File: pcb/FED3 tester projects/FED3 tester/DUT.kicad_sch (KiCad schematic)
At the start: 68 parts, among them J3 6pin_hd, J4 Conn_02x03_Odd_Even, J5 MotorCkeck1, J6 MotorCkeck2, J7 Conn_01x02_Socket, K1 Relay SPDT, K2 Relay SPDT, K3 Relay SPDT, Q2 ???????, Q3 DMN63D8L-7, Q4 DMN63D8L-7, Q5 DMN63D8L-7, Q6 DMN63D8L-7, U6 THS4281, U7 THS4281, U8 THS4281, U9 ZXCT1082

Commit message: FED3 tester - sync of the week
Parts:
- added R39: 640k, Resistor_SMD:R_0402_1005Metric, symbol Device:R_US
- added R42: 1M, Resistor_SMD:R_0402_1005Metric, symbol Device:R_US
- R29: value 1.2K -> 1.2K ??
- renumbered C31 to C30, C32 to C31, C33 to C32, C34 to C33, C35 to C34, C36 to C35, C37 to C36, C38 to C37, C39 to C38, R39 to R40, R40 to R41, R41 to R43, R42 to R44, R43 to R45, R44 to R46, R45 to R47, R46 to R48
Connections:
- net GND: now also R42.1
- net LED_CHG: now also R39.1, R42.2; no longer TP10.1
- new net: R39.2, TP10.1
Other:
- moved on the sheet: TP6

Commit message: FED3 tester rev.B & FED3 tester support rev.B
-rev.B para 1ª revisão do Filipe
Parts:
- Q2: value ??????? -> PMF170XP,115; footprint Package_TO_SOT_SMD:SOT-23 -> Package_TO_SOT_SMD:SOT-323_SC-70; MPN (none) -> PMF170XP,115; OEPSPN (none) -> OEPS060012
- renumbered C30 to C29, C31 to C30, C32 to C31, C33 to C32, C34 to C33, C35 to C34, C36 to C35, C37 to C36, C38 to C37, D11 to D10, D12 to D11, D10 to D9, R19 to R18, R20 to R19, R21 to R20, R22 to R21, R23 to R22, R24 to R23, R25 to R24, R26 to R25, R27 to R26, R28 to R27, R29 to R28, R30 to R29, R31 to R30, R32 to R31, R33 to R32, R34 to R33, R35 to R34, R36 to R35, R37 to R36, R38 to R37, R39 to R38, R40 to R39, R41 to R40, R42 to R41, R43 to R42, R44 to R43, R45 to R44, R46 to R45, R47 to R46, R48 to R47
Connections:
- net +3V3test renamed +3V3_DUT
- net DUT_SWCLK renamed SWCLK_DUT
- net DUT_SWDIO renamed SWDIO_DUT
- net ExtVUSB renamed ExtVUSB_DUT
- net ThermalPin renamed ThermalPin_DUT
- net VBattest renamed VBatt_DUT
- net VUSB_out renamed VUSB_DUT
- net VccRGB renamed VccRGB_DUT

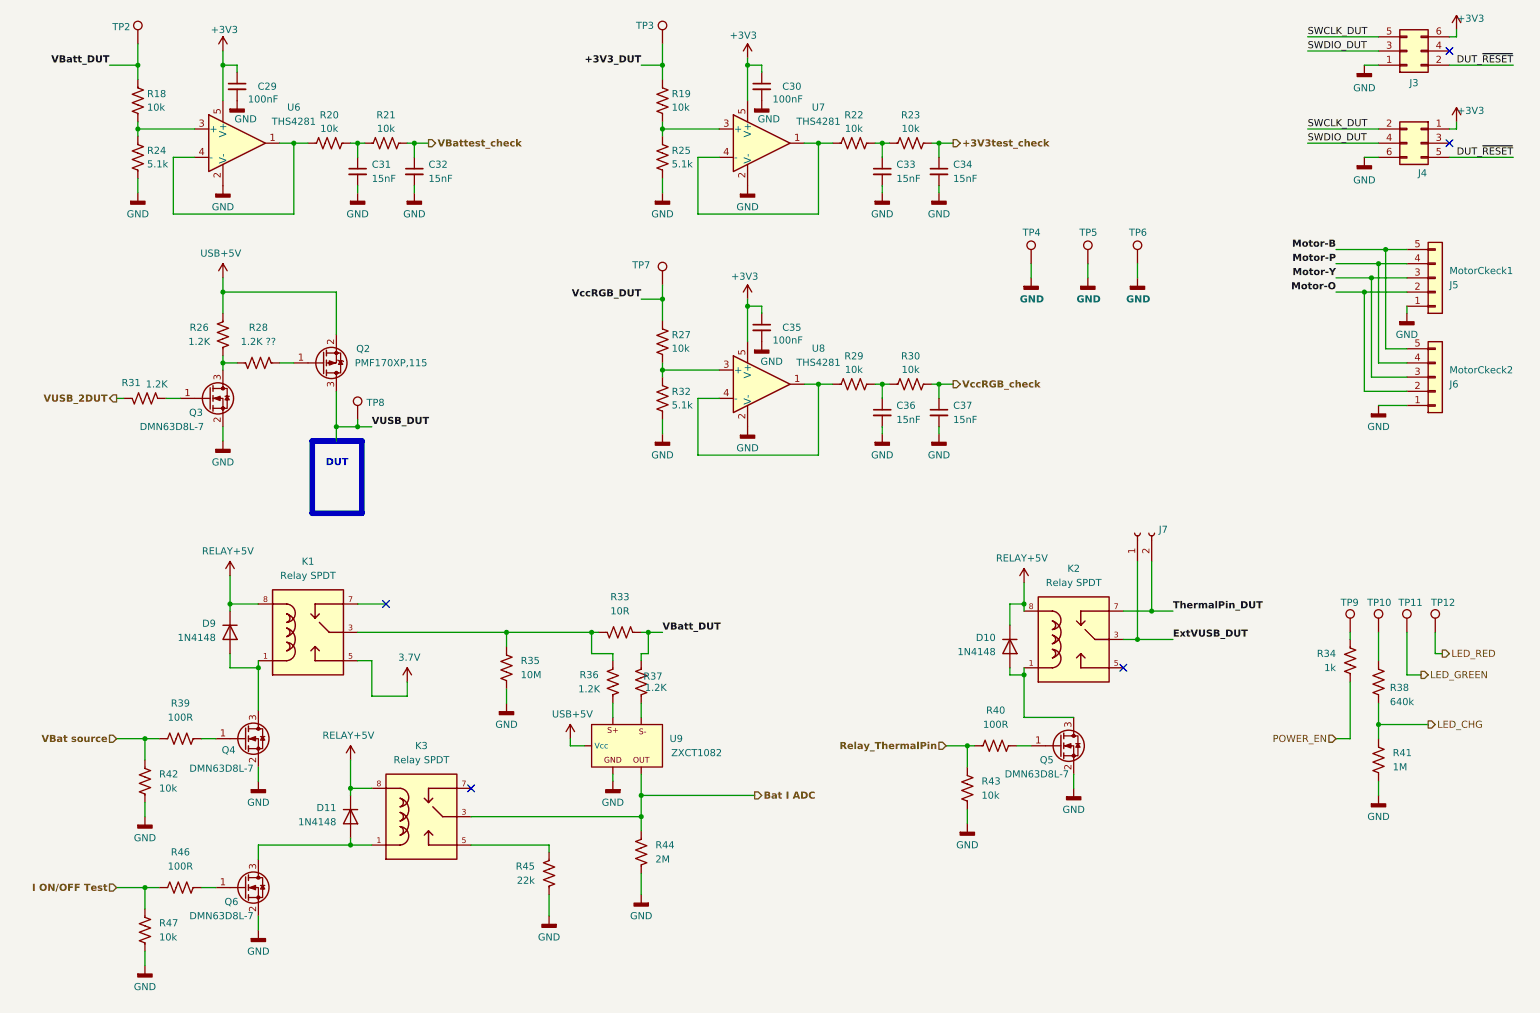
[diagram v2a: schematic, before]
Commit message: completos OEPSPN & MPN
- andar de I-measure  ZXCT1086 redimensionado
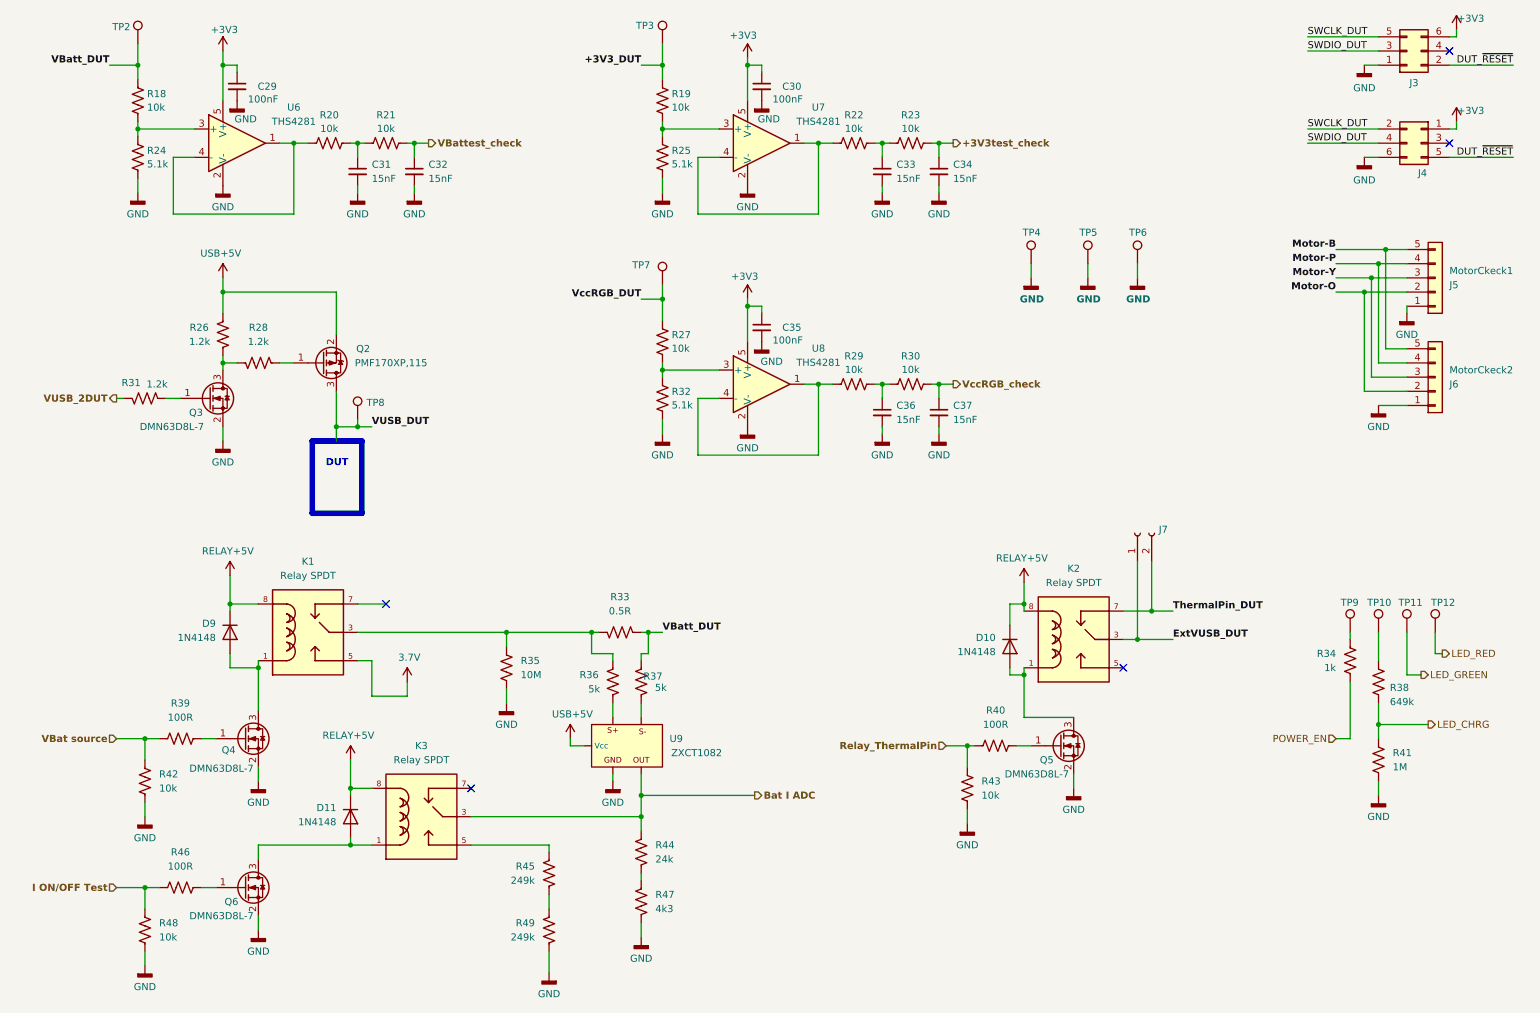
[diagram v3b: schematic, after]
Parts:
- added R47: 4k3, Resistor_SMD:R_0603_1608Metric, symbol Device:R_US
- added R49: 249k, Resistor_SMD:R_0402_1005Metric, symbol Device:R_US
- R26, R31: value 1.2K -> 1.2k
- R28: value 1.2K ?? -> 1.2k
- R33: value 10R -> 0.5R; footprint Resistor_SMD:R_0402_1005Metric -> Resistor_SMD:R_0805_2012Metric; MPN ERJ-PA2J100X -> RL1220S-R50-F; OEPSPN OEPS020041 -> OEPS020221; Tolerance 5% -> 1%
- R36, R37: value 1.2K -> 5k; MPN ERA-2AEB122X -> PNM0402E5001BST1; OEPSPN OEPS020213 -> OEPS020206
- R38: value 640k -> 649k; MPN tbd -> ERJ-2RKF6493X; OEPSPN tbd -> OEPS020022
- R41: MPN tbd -> CRCW04021M00FKED; OEPSPN tbd -> OEPS020026
- R44: value 2M -> 24k; MPN CRCW04022M00FKEDC -> ERJ-2RKF2402X; OEPSPN OEPS020210 -> OEPS020048
- R45: value 22k -> 249k; MPN ERA-2AEB223X -> RMCF0402FT249K; OEPSPN OEPS020212 -> OEPS020209
- renumbered R47 to R48
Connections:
- net GND: now also R47.2, R49.1; no longer R44.2, R45.1
- net LED_CHG renamed LED_CHRG
- new net: R45.1, R49.2
- new net: R44.2, R47.1

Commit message: revistos OEPSPN & MPN com gsheet - OK
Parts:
- J4: MPN 61300511021 -> 61300621021; OEPSPN OEPS070143 -> OEPS070144
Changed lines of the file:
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@@
 			)
 		)
-		(property "Description" "SMD 0402 1kΩ ±1% 0.063W"
+		(property "Description" "SMD 0402 1MΩ ±1% 0.063W"
 			(at 255.27 152.4 0)
 			(hide yes)
@@
 			)
 		)
-		(property "Description" ""
+		(property "Description" "HEADER 2.54MM R/A 2x3POS"
 			(at 262.89 41.91 0)
 			(hide yes)
@@
 			)
 		)
-		(property "MPN" "61300511021"
+		(property "MPN" "61300621021"
 			(at 258.318 48.006 0)
 			(hide yes)
@@
 			)
 		)
-		(property "OEPSPN" "OEPS070143"
+		(property "OEPSPN" "OEPS070144"
 			(at 262.89 41.91 0)
 			(hide yes)
